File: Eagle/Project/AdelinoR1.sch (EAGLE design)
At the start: 67 parts, among them J1 DC-044-A, J2 YELLOW-8P-2.54, J3 YELLOW-6P-2.54, J4 YELLOW-8P-2.54, J5 YELLOW-8P-2.54, J6 4P-2.0, J7 YELLOW-2X3P-2.54, J8 4P-2.0, Q1 NCE3407A, Q2 CJ2305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

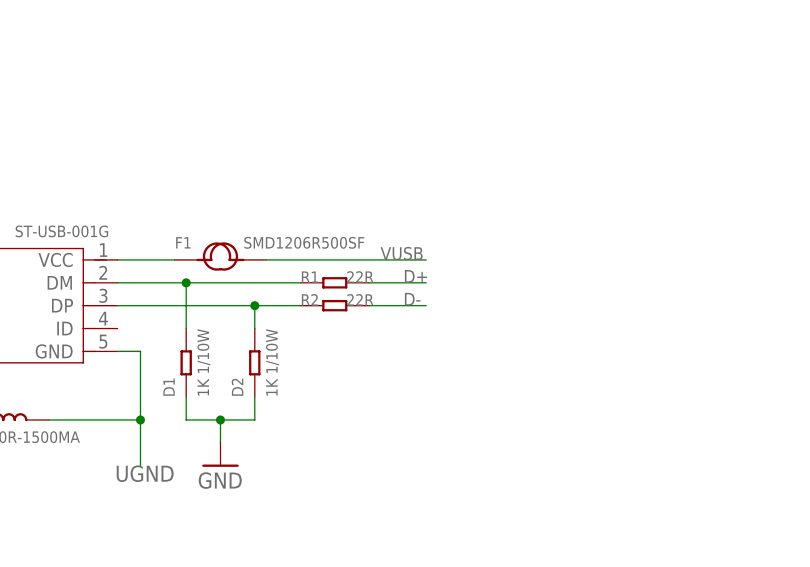
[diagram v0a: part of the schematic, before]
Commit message: Fix USB connector D+/D- wiring.
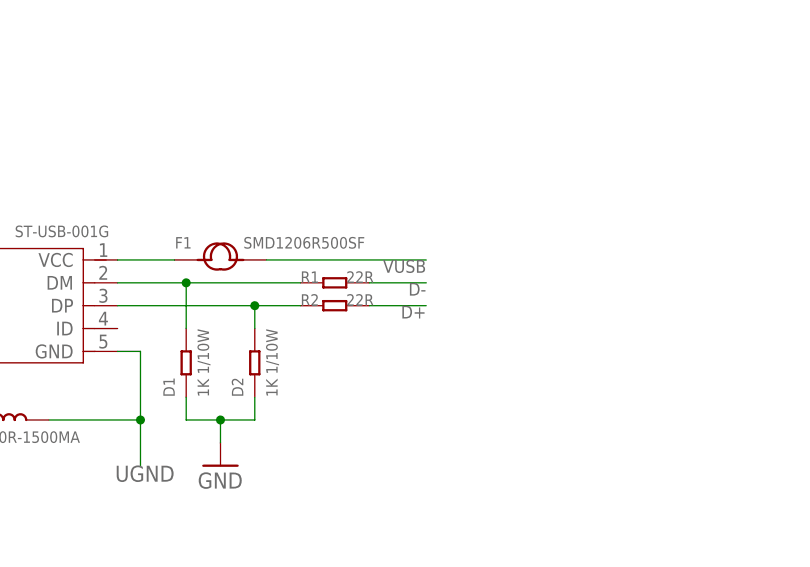
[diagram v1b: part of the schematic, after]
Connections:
- net D+: now also R2.2; no longer R1.2
- net D-: now also R1.2; no longer R2.2
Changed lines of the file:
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@@
 <?xml version="1.0" encoding="utf-8"?>
 <!DOCTYPE eagle SYSTEM "eagle.dtd">
-<eagle version="9.2.1">
+<eagle version="9.2.2">
 <drawing>
 <settings>
@@
 <net name="D+" class="0">
 <segment>
-<pinref part="R1" gate="G$1" pin="2"/>
-<wire x1="-166.37" y1="142.24" x2="-160.02" y2="142.24" width="0.1524" layer="91"/>
-<label x="-162.56" y="142.24" size="1.4224" layer="95"/>
-</segment>
-<segment>
 <pinref part="U4" gate="G$1" pin="D+"/>
 <wire x1="85.09" y1="100.33" x2="72.39" y2="100.33" width="0.1524" layer="91"/>
 <label x="72.39" y="100.33" size="1.778" layer="95"/>
 </segment>
+<segment>
+<pinref part="R2" gate="G$1" pin="2"/>
+<wire x1="-166.37" y1="139.7" x2="-160.02" y2="139.7" width="0.1524" layer="91"/>
+<label x="-160.02" y="139.7" size="1.4224" layer="95" rot="R180"/>
+</segment>
 </net>
 <net name="D-" class="0">
-<segment>
-<pinref part="R2" gate="G$1" pin="2"/>
-<wire x1="-166.37" y1="139.7" x2="-160.02" y2="139.7" width="0.1524" layer="91"/>
-<label x="-162.56" y="139.7" size="1.4224" layer="95"/>
-</segment>
 <segment>
 <pinref part="U4" gate="G$1" pin="D-"/>
 <wire x1="85.09" y1="97.79" x2="72.39" y2="97.79" width="0.1524" layer="91"/>
 <label x="72.39" y="97.79" size="1.778" layer="95"/>
+</segment>
+<segment>
+<pinref part="R1" gate="G$1" pin="2"/>
+<wire x1="-166.37" y1="142.24" x2="-160.02" y2="142.24" width="0.1524" layer="91"/>
+<label x="-160.02" y="142.24" size="1.4224" layer="95" rot="R180"/>
 </segment>
 </net>
@@
 <pinref part="F1" gate="G$1" pin="2"/>
 <wire x1="-177.8" y1="144.78" x2="-160.02" y2="144.78" width="0.1524" layer="91"/>
-<label x="-165.1" y="144.78" size="1.4224" layer="95"/>
-</segment>
-<segment>
+<label x="-160.02" y="144.78" size="1.4224" layer="95" rot="R180"/>
+</segment>
+<segment>
